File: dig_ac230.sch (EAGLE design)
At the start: 142 parts, among them IC201 ATMEGA32A-AU, IC202 DS1337S, IC203 MAX487CSA, IC204 74HC166D, IC301 LTV-356T, IC302 LTV-356T, IC303 LTV-356T, IC304 LTV-356T, IC305 LTV-356T, IC306 LTV-356T, IC307 LTV-356T, IC308 LTV-356T, IC401 74HC595D, K401 S202S02, K402 S202S02, K403 S202S02, K404 S202S02, K405 S202S02, K406 S202S02, K407 S202S02, K408 S202S02, Q201 32,768kHz, Q301 BCR191, Q302 BCR191, Q303 BCR191, Q304 BCR191, Q305 BCR191, Q306 BCR191, Q307 BCR191, Q308 BCR191, X101 RIA-73-02, X201 ISP, X202 RIA-73-02, X301 RIA-73-02, X302 RIA-73-02, X303 RIA-73-02, X304 RIA-73-02, X305 RIA-73-02, X401 RIA-73-02, X402 RIA-73-02, X403 RIA-73-02, X404 RIA-73-02, X405 RIA-73-02

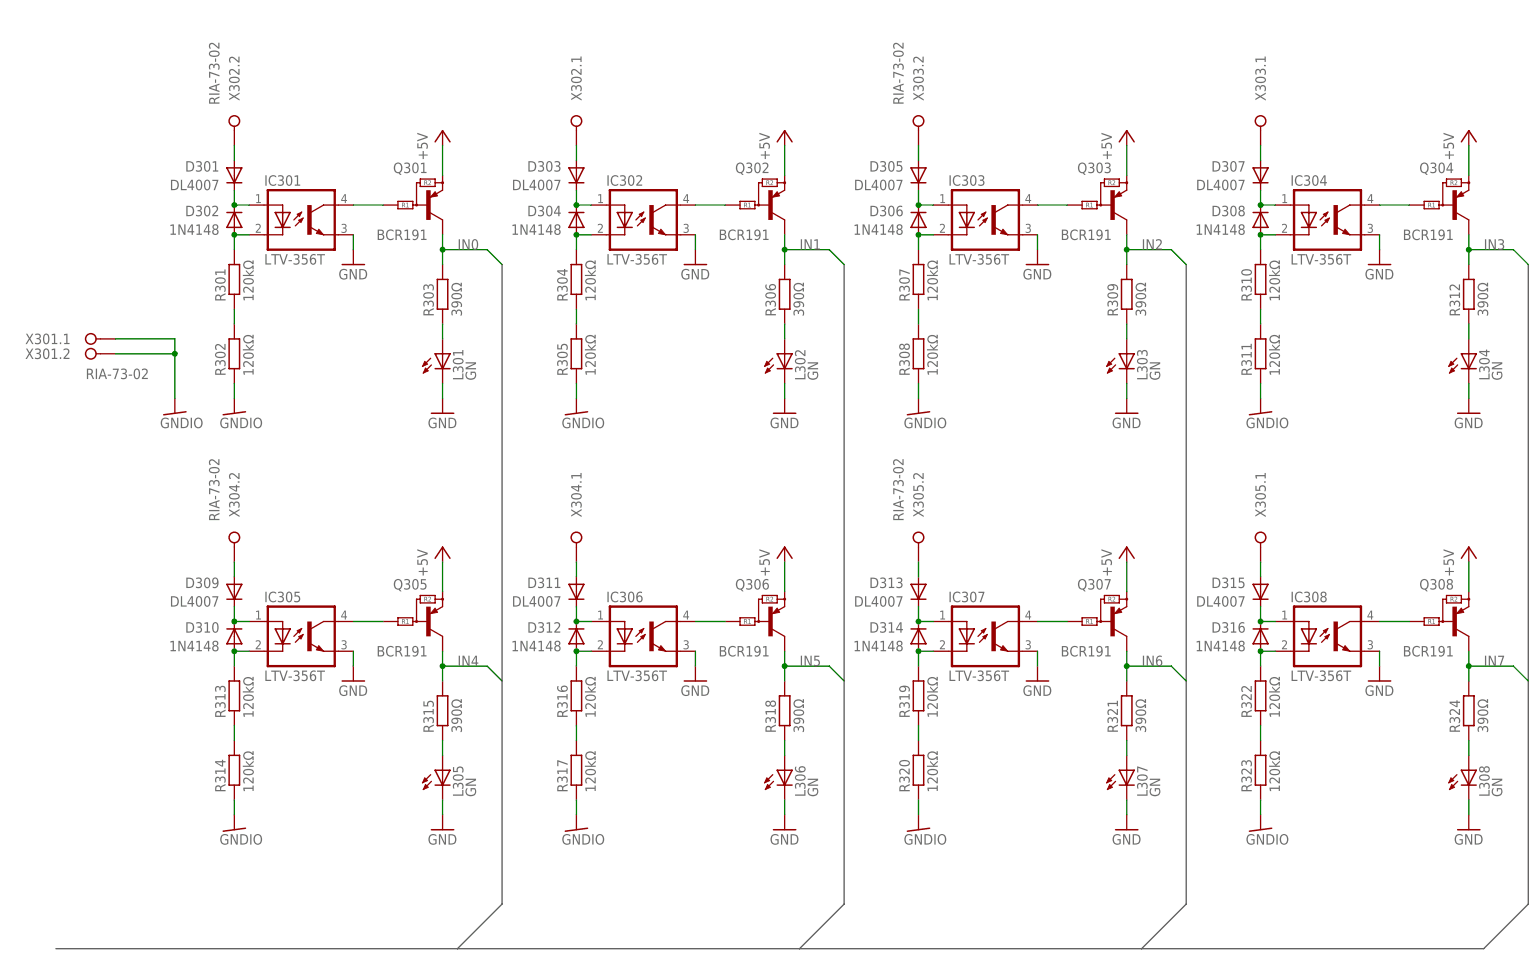
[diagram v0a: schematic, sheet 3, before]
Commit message: Eingänge auf ltv-354t umgestellt
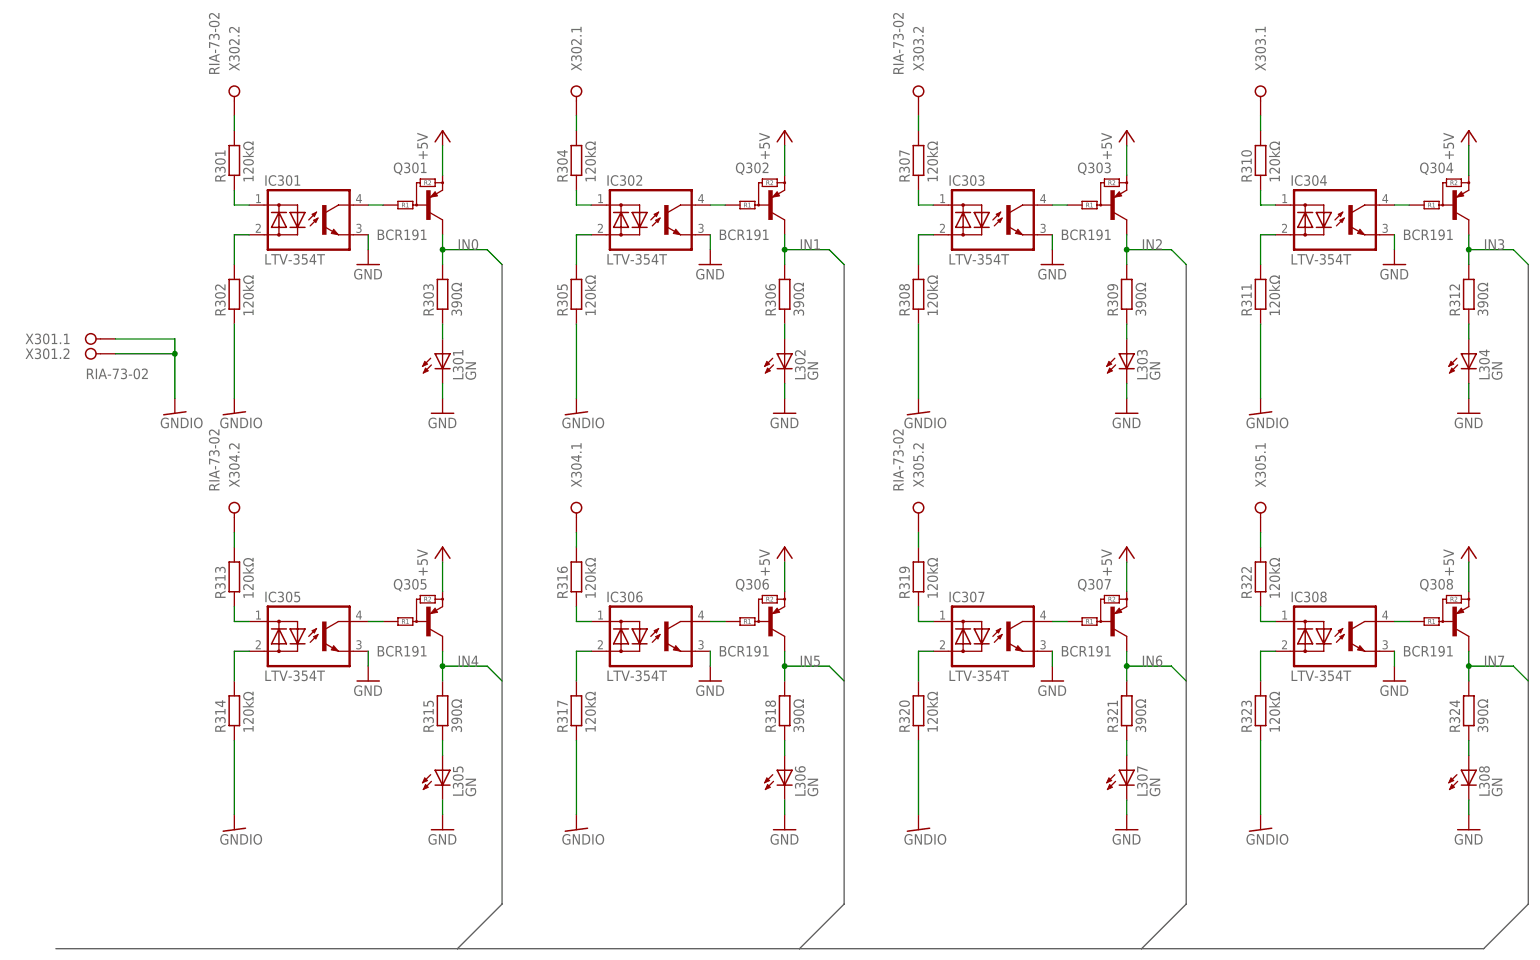
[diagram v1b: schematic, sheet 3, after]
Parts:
- removed D301, D303, D305, D307, D309, D311, D313, D315: DL4007, diode:DIODE-MELF
- removed D302, D304, D306, D308, D310, D312, D314, D316: 1N4148, diode:DIODE-MINIMELF
- IC301, IC302, IC303, IC304, IC305, IC306, IC307, IC308: value LTV-356T -> LTV-354T; device ic-optokoppler:LTV-356T -> ic-optokoppler:LTV-354T
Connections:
- removed net N$100: D313.A, X305.2.A
- removed net N$101: D315.A, X305.1.A
- removed net N$86: D301.A, X302.2.A
- removed net N$87: D303.A, X302.1.A
- removed net N$88: D305.A, X303.2.A
- removed net N$91: D307.A, X303.1.A
- removed net N$94: D309.A, X304.2.A
- removed net N$97: D311.A, X304.1.A
- net N$1: now also R301.2, X302.2.A; no longer D301.K, D302.K, IC301.A
- net N$10: now also R310.2, X303.1.A; no longer D310.A, IC305.K, R313.2
- net N$11: now also IC304.A, R310.1; no longer D311.K, D312.K, IC306.A
- net N$12: now also IC304.K, R311.2; no longer D312.A, IC306.K, R316.2
- net N$13: now also R313.2, X304.2.A; no longer D313.K, D314.K, IC307.A
- net N$14: now also IC305.A, R313.1; no longer D314.A, IC307.K, R319.2
- net N$15: now also IC305.K, R314.2; no longer D315.K, D316.K, IC308.A
- net N$16: now also R316.2, X304.1.A; no longer D316.A, IC308.K, R322.2
- net N$2: now also IC301.A, R301.1; no longer D302.A, IC301.K, R301.2
- net N$3: now also IC301.K, R302.2; no longer D303.K, D304.K, IC302.A
- net N$35: now also IC306.A, R316.1; no longer R301.1, R302.2
- net N$37: now also IC306.K, R317.2; no longer R304.1, R305.2
- net N$39: now also IC307.A, R319.1; no longer R307.1, R308.2
- net N$4: now also X302.1.A; no longer D304.A, IC302.K
- net N$5: now also IC302.A, R304.1; no longer D305.K, D306.K, IC303.A
- net N$50: now also IC307.K, R320.2; no longer R310.1, R311.2
- net N$57: now also R319.2, X305.2.A; no longer R313.1, R314.2
- net N$6: now also IC302.K, R305.2; no longer D306.A, IC303.K, R307.2
- net N$67: now also R322.2, X305.1.A; no longer R316.1, R317.2
- net N$7: now also R307.2, X303.2.A; no longer D307.K, D308.K, IC304.A
- net N$71: now also IC308.A, R322.1; no longer R319.1, R320.2
- net N$79: now also IC308.K; no longer R322.1
- net N$8: now also IC303.A, R307.1; no longer D308.A, IC304.K, R310.2
- net N$9: now also IC303.K, R308.2; no longer D309.K, D310.K, IC305.A
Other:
- moved on the sheet: R301, R302, R304, R305, R307, R308, R310, R311, R313, R314, R316, R317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

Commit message: Bezeichnungen angepasst; Position auf Board angepasst
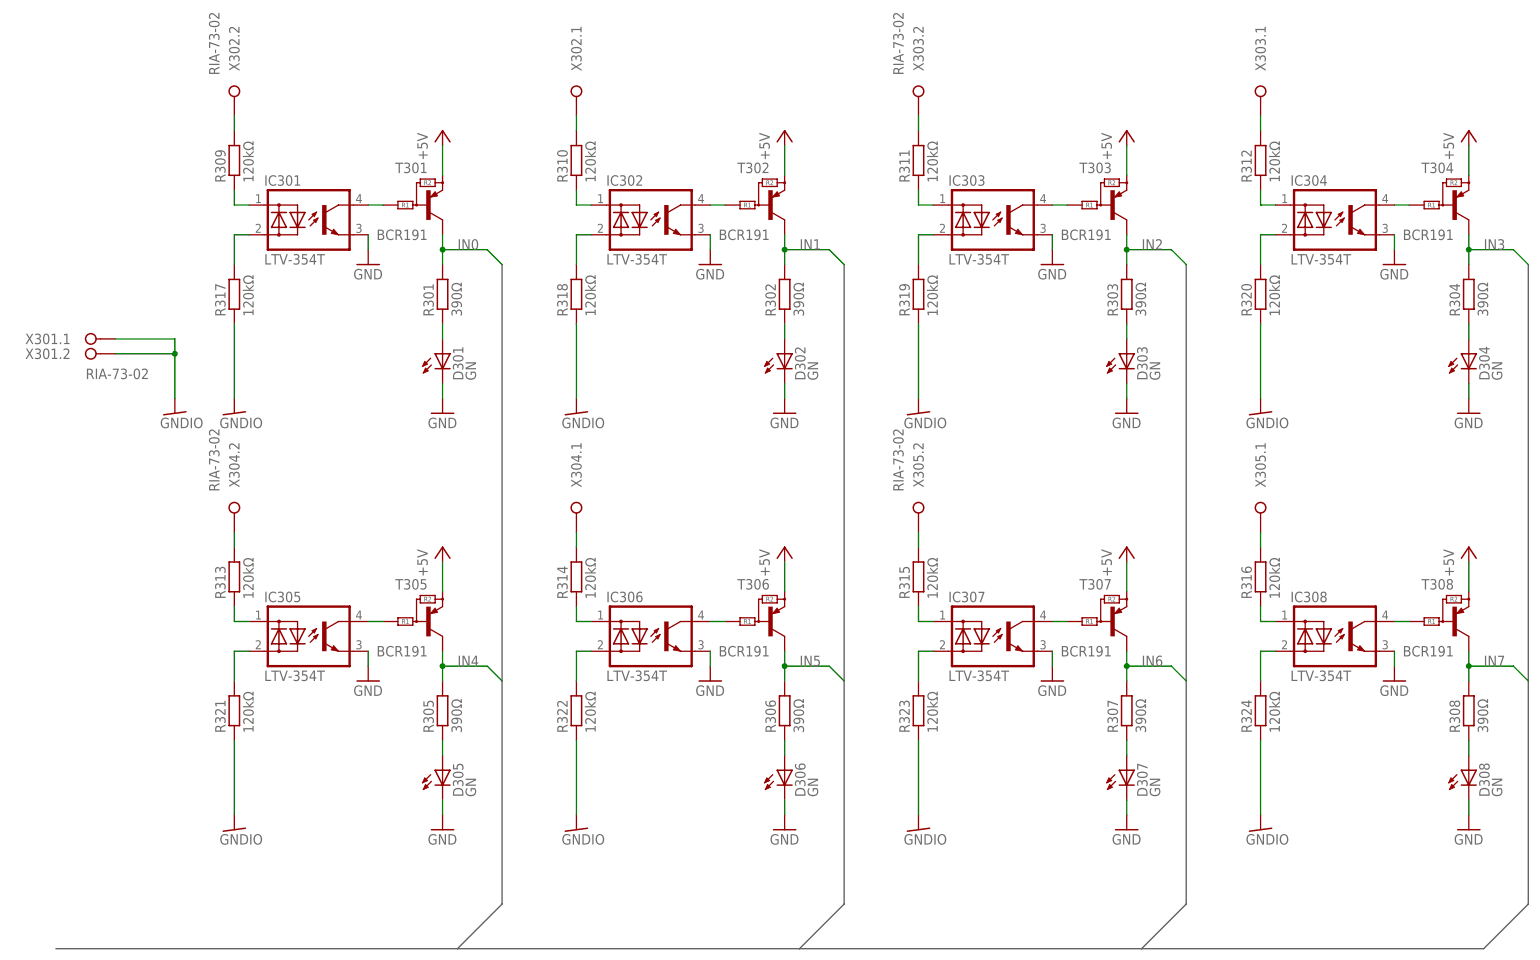
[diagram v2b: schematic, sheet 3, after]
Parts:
- removed L101: GN, led:LED3MM
- removed V101: TME2405S, schaltregler:TME2405S
- added D104: 1N4148, diode:DIODE-MINIMELF
- added G102: KZH20P, batterie:KZH20P
- D102: value 1N4148 -> GN; device diode:DIODE-MINIMELF -> led:LED3MM
- G101: value KZH20P -> TME2405S; device batterie:KZH20P -> schaltregler:TME2405S; MPN (none) -> TME 2405S; OC_FARNELL (none) -> 1007547; OC_NEWARK (none) -> 51R5329
- R301, R302, R304, R305, R307, R308: value 120kΩ -> 390Ω; device passiv:R_1206 -> passiv:R_0805
- R309, R312, R315, R318, R321, R324: value 390Ω -> 120kΩ; device passiv:R_0805 -> passiv:R_1206
- renumbered L201 to D201, L202 to D202, L301 to D301, L302 to D302, L303 to D303, L304 to D304, L305 to D305, L306 to D306, L307 to D307, L308 to D308, L401 to D401, L402 to D402, L403 to D403, L404 to D404, L405 to D405, L406 to D406, L407 to D407, L408 to D408, Q301 to T301, Q302 to T302, Q303 to T303, Q304 to T304, Q305 to T305, Q306 to T306, Q307 to T307, Q308 to T308
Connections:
- net +5V: now also D103.A; no longer D102.A
- net GND: now also D102.C, G101.-VOUT, G102.-; no longer G101.-, L101.C, V101.-VOUT
- net GNDIO: now also R318.1, R319.1, R321.1, R322.1, R324.1; no longer R302.1, R305.1, R308.1, R311.1, R314.1
- net IN0: now also R301.2; no longer R303.2
- net IN1: now also R302.2; no longer R306.2
- net IN2: now also R303.2; no longer R309.2
- net IN3: now also R304.2; no longer R312.2
- net IN4: now also R305.2; no longer R315.2
- net IN5: now also R306.2; no longer R318.2
- net IN6: now also R307.2; no longer R321.2
- net IN7: now also R308.2; no longer R324.2
- net N$1: now also R309.2; no longer R301.2
- net N$10: now also R312.2; no longer R310.2
- net N$11: now also R312.1; no longer R310.1
- net N$12: now also R320.2; no longer R311.2
- net N$15: now also R321.2; no longer R314.2
- net N$16: now also R314.2; no longer R316.2
- net N$19: now also G101.-VIN; no longer V101.-VIN
- net N$2: now also R309.1; no longer R301.1
- net N$21: now also D104.A, G102.+; no longer D103.A, G101.+
- net N$23: now also G101.+VIN; no longer V101.+VIN
- net N$3: now also R317.2; no longer R302.2
- net N$34: now also R304.1; no longer R312.1
- net N$35: now also R314.1; no longer R316.1
- net N$36: now also R303.1; no longer R309.1
- net N$37: now also R322.2; no longer R317.2
- net N$38: now also R302.1; no longer R306.1
- net N$39: now also R315.1; no longer R319.1
- net N$4: now also R310.2; no longer R304.2
- net N$40: now also R301.1; no longer R303.1
- net N$41: now also G101.+VOUT; no longer V101.+VOUT
- net N$44: now also D102.A; no longer L101.A
- net N$5: now also R310.1; no longer R304.1
- net N$50: now also R323.2; no longer R320.2
- net N$55: now also R305.1; no longer R315.1
- net N$57: now also R315.2; no longer R319.2
- net N$6: now also R318.2; no longer R305.2
- net N$64: now also D104.K; no longer D102.K
- net N$65: now also R306.1; no longer R318.1
- net N$67: now also R316.2; no longer R322.2
- net N$69: now also R307.1; no longer R321.1
- net N$7: now also R311.2; no longer R307.2
- net N$71: now also R316.1; no longer R322.1
- net N$77: now also R308.1; no longer R324.1
- net N$79: now also R324.2; no longer R323.2
- net N$8: now also R311.1; no longer R307.1
- net N$9: now also R319.2; no longer R308.2
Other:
- moved on the sheet: D103, R301, R302, R303, R304, R305, R306, R307, R308, R309, R310, R311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

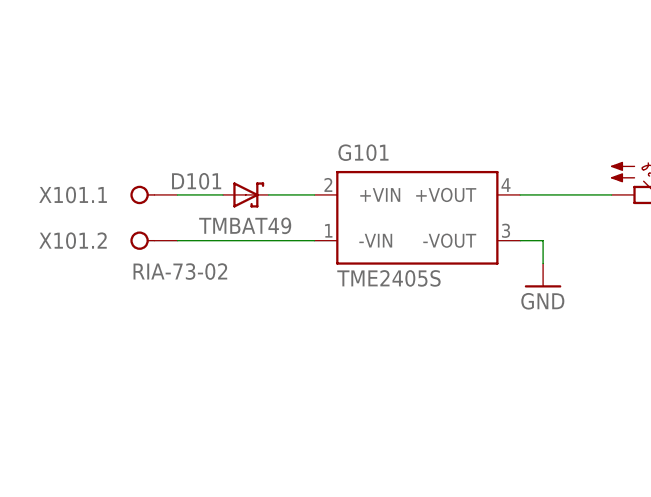
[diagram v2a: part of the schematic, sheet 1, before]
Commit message: Wert von D101 geändert
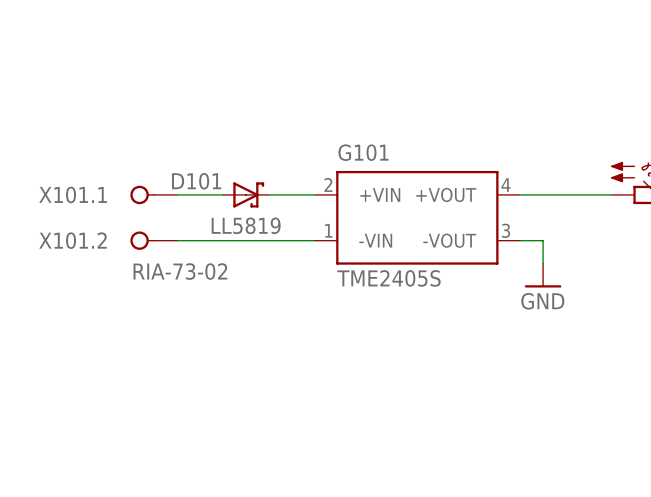
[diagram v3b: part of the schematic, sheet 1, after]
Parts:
- D101: value TMBAT49 -> LL5819
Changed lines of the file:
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@@
 <attribute name="OC_NEWARK" value="51R5329"/>
 </part>
-<part name="D101" library="diode" deviceset="SHOTKY-DIODE" device="-MELF" value="TMBAT49"/>
+<part name="D101" library="diode" deviceset="SHOTKY-DIODE" device="-MELF" value="LL5819"/>
 <part name="D102" library="led" deviceset="LED" device="3MM" value="GN"/>
 <part name="R101" library="passiv" deviceset="R_" device="0805" value="390Ω"/>
